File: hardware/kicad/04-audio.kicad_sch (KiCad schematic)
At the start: 9 parts, among them U5 PAM8403

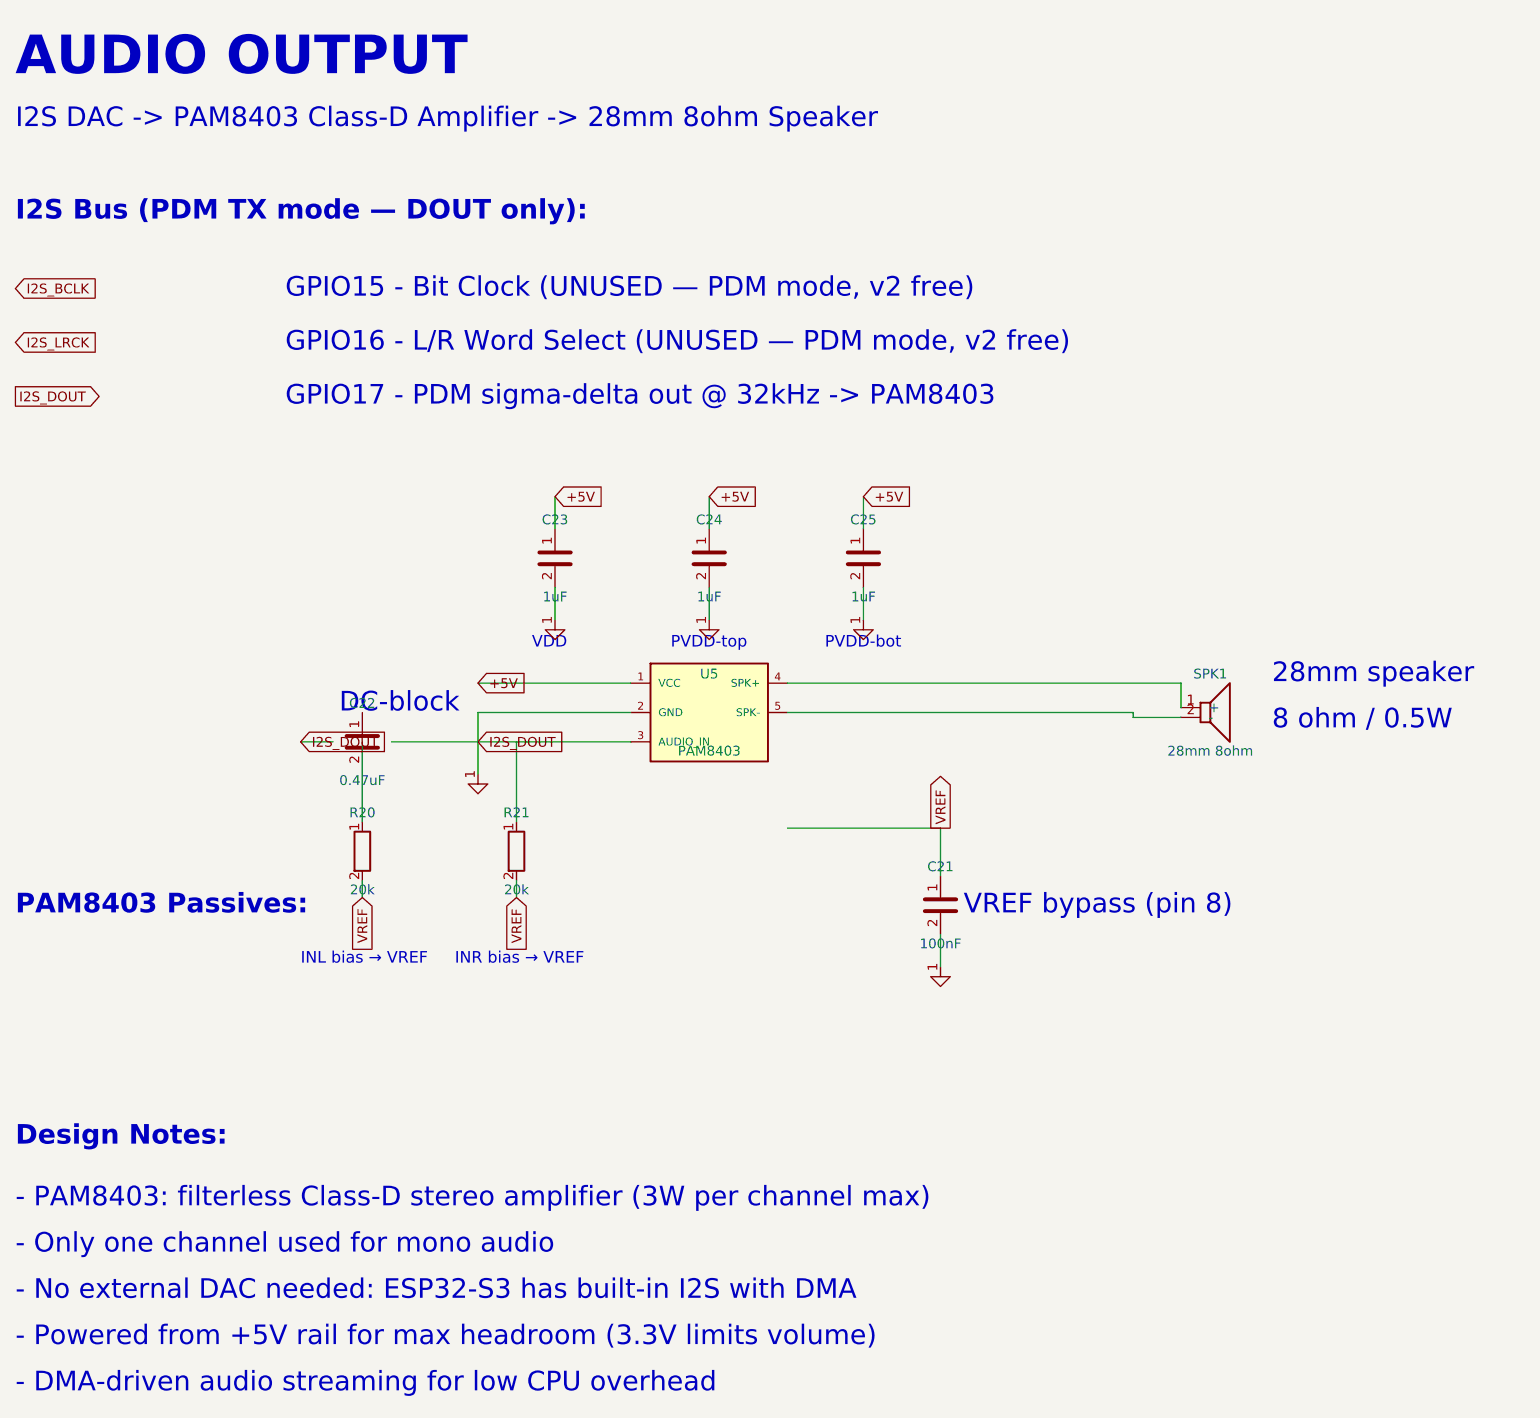
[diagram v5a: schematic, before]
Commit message: fix(pcb): R5-CRIT-6 relocate D1 so the menu combo works + split I2S_DOUT/PAM_IN_AC
Two long-standing tech-debt items, both of which were hiding real DRC
signal behind permanently-accepted "unconnected" entries.

1) R5-CRIT-6 — D1 menu-combo diode had both anodes isolated
--------------------------------------------------------------
Root cause was the placement, not the routing. D1 sat at (156, 52.5)
next to SW13, but BTN_START and BTN_SELECT both terminate around
x=100-102 and no corridor reaches x=156: the south perimeter at
y=73.955 crosses the J1 USB-C back-row shield pads (y=[72.575,74.575]),
and the north path is blocked by IP5306, L1, the regulator, the C17-C19
pads, the MENU_K F.Cu at x=156 and the USB_D+/D- verticals at x=90-91.
Previous sessions tried to route out of that position and failed.

Fix: move D1 to the buttons so only ONE net has to cross the board.

  D1 -> (101.225, 56.5), KiCad rotation 180 deg, B.Cu — the 1.30 mm free
  channel between the BTN_START column (x=100.45) and the BTN_SELECT
  column (x=102.00). At 180 deg the SOT-23 two-pad row faces north, so
  pin 1 lands on the west column and pin 2 on the east column with no
  crossing.

    D1.1 (100.275, 55.400) -> 0.175 mm B.Cu stub east onto x=100.45.
         The BTN_START vertical is split at y=55.400 so the tap is a
         real 3-way junction, not a branch into a segment middle.
    D1.2 (102.175, 55.400) -> 0.175 mm B.Cu stub west onto x=102.00,
         and the BTN_SELECT column is extended north from y=60.00.
    D1.3 (101.225, 57.600) -> B.Cu south to (101.225, 62.400) -> via ->
         F.Cu east at y=62.400 to x=137.0 -> north to y=59.850 -> east
         across SW13 pads 1 and 2.

  The SW13 pad-3 GND via moved from (135.0, 61.55) to (135.0, 63.55):
  its 2 mm F.Cu riser occupied x=[134.85,135.15], y=[61.40,63.70] —
  straight across the only usable MENU_K corridor.

  Everything stays west of x=105 in the y=[39,59] band so it does not
  collide with the parallel SY8089A buck-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
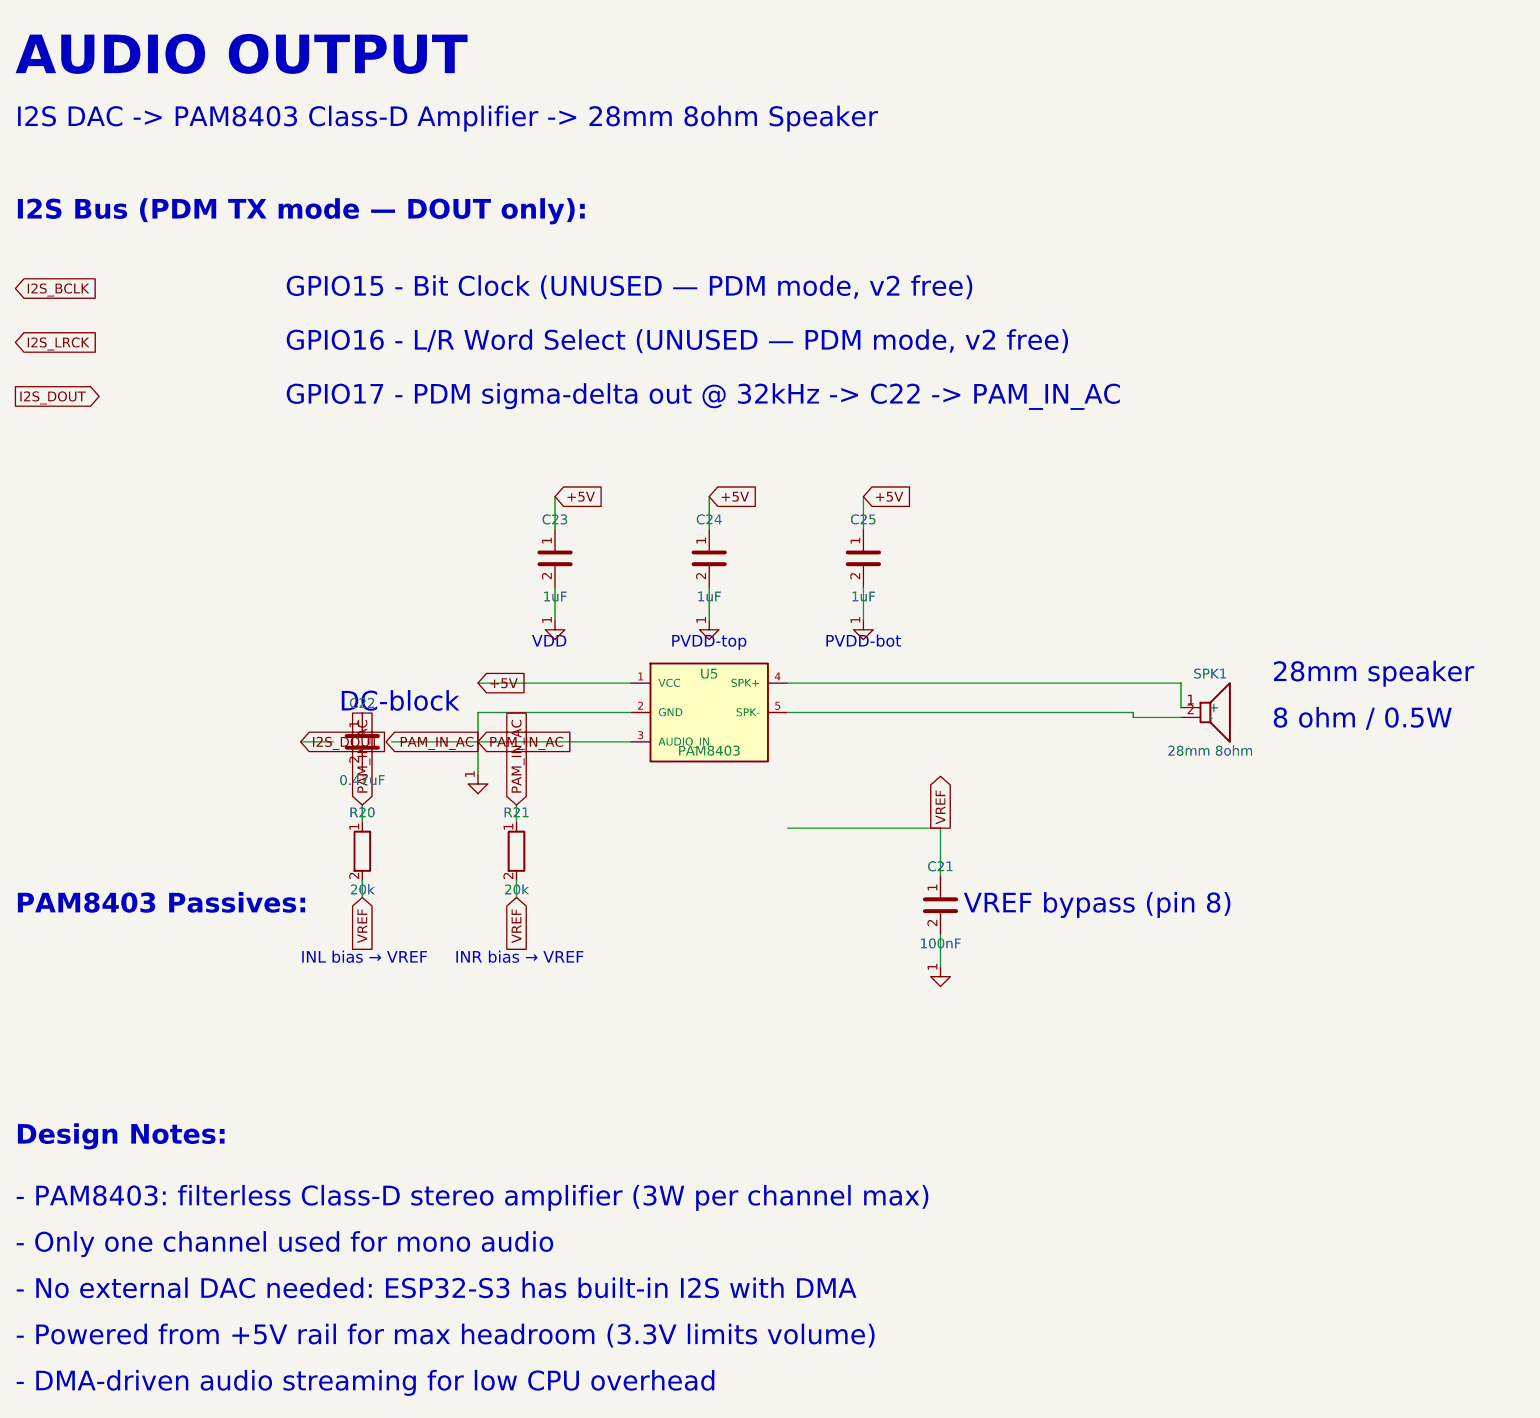
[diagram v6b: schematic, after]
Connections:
- net I2S_DOUT: no longer U5.2 (GND), U5.3 (AUDIO_IN)
- net PAM_IN_AC: now reaches R20.1
- net PAM_IN_AC: now also R21.1, U5.2 (GND), U5.3 (AUDIO_IN)
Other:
- note added: "GPIO17 - PDM sigma-delta out @ 32kHz -> C22 -> PAM_IN_AC"
- note removed: "GPIO17 - PDM sigma-delta out @ 32kHz -> PAM8403"
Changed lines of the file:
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@@
   (wire (pts (xy 109.84 110) (xy 90 110)) (stroke (width 0) (type default)))
   (wire (pts (xy 90 110) (xy 90 118)) (stroke (width 0) (type default)))
-  (global_label "I2S_DOUT" (shape input) (at 90 113.81 0) (effects (font (size 1.27 1.27))) (property "Intersheetrefs" "" (at 0 0 0) (effects (font (size 1.27 1.27)) hide)))
+  (global_label "PAM_IN_AC" (shape input) (at 90 113.81 0) (effects (font (size 1.27 1.27))) (property "Intersheetrefs" "" (at 0 0 0) (effects (font (size 1.27 1.27)) hide)))
   (wire (pts (xy 90 113.81) (xy 109.84 113.81)) (stroke (width 0) (type default)))
   (text "I2S Bus (PDM TX mode — DOUT only):" (at 30 45 0) (effects (font (size 2.54 2.54) bold) (justify left)))
@@
   (text "GPIO16 - L/R Word Select (UNUSED — PDM mode, v2 free)" (at 65 62 0) (effects (font (size 2.54 2.54)) (justify left)))
   (global_label "I2S_DOUT" (shape output) (at 30 69 0) (effects (font (size 1.27 1.27))) (property "Intersheetrefs" "" (at 0 0 0) (effects (font (size 1.27 1.27)) hide)))
-  (text "GPIO17 - PDM sigma-delta out @ 32kHz -> PAM8403" (at 65 69 0) (effects (font (size 2.54 2.54)) (justify left)))
+  (text "GPIO17 - PDM sigma-delta out @ 32kHz -> C22 -> PAM_IN_AC" (at 65 69 0) (effects (font (size 2.54 2.54)) (justify left)))
   (symbol (lib_id "Speaker") (at 185 110 0) (unit 1) (exclude_from_sim no) (in_bom yes) (on_board yes) (dnp no) (property "Reference" "SPK1" (at 185 105 0) (effects (font (size 1.27 1.27)))) (property "Value" "28mm 8ohm" (at 185 115 0) (effects (font (size 1.27 1.27)))) (pin "1") (pin "2"))
   (text "28mm speaker" (at 193 105 0) (effects (font (size 2.54 2.54)) (justify left)))
@@
   (symbol (lib_id "C") (at 75 113.81 0) (unit 1) (exclude_from_sim no) (in_bom yes) (on_board yes) (dnp no) (property "Reference" "C22" (at 75 108.81 0) (effects (font (size 1.27 1.27)))) (property "Value" "0.47uF" (at 75 118.81 0) (effects (font (size 1.27 1.27)))) (pin "1") (pin "2"))
   (wire (pts (xy 78.81 113.81) (xy 90 113.81)) (stroke (width 0) (type default)))
+  (global_label "PAM_IN_AC" (shape output) (at 90 113.81 180) (effects (font (size 1.27 1.27))) (property "Intersheetrefs" "" (at 0 0 0) (effects (font (size 1.27 1.27)) hide)))
   (wire (pts (xy 71.19 113.81) (xy 67 113.81)) (stroke (width 0) (type default)))
   (global_label "I2S_DOUT" (shape input) (at 67 113.81 0) (effects (font (size 1.27 1.27))) (property "Intersheetrefs" "" (at 0 0 0) (effects (font (size 1.27 1.27)) hide)))
   (text "DC-block" (at 72 108.81 0) (effects (font (size 2.54 2.54)) (justify left)))
   (symbol (lib_id "R") (at 75 128 0) (unit 1) (exclude_from_sim no) (in_bom yes) (on_board yes) (dnp no) (property "Reference" "R20" (at 75 123 0) (effects (font (size 1.27 1.27)))) (property "Value" "20k" (at 75 133 0) (effects (font (size 1.27 1.27)))) (pin "1") (pin "2"))
-  (wire (pts (xy 75 124.19) (xy 75 113.81)) (stroke (width 0) (type default)))
+  (wire (pts (xy 75 124.19) (xy 75 122)) (stroke (width 0) (type default)))
+  (global_label "PAM_IN_AC" (shape input) (at 75 122 90) (effects (font (size 1.27 1.27))) (property "Intersheetrefs" "" (at 0 0 0) (effects (font (size 1.27 1.27)) hide)))
   (wire (pts (xy 75 131.81) (xy 75 134)) (stroke (width 0) (type default)))
   (global_label "VREF" (shape input) (at 75 134 270) (effects (font (size 1.27 1.27))) (property "Intersheetrefs" "" (at 0 0 0) (effects (font (size 1.27 1.27)) hide)))
   (text "INL bias → VREF" (at 67 142 0) (effects (font (size 1.5 1.5)) (justify left)))
   (symbol (lib_id "R") (at 95 128 0) (unit 1) (exclude_from_sim no) (in_bom yes) (on_board yes) (dnp no) (property "Reference" "R21" (at 95 123 0) (effects (font (size 1.27 1.27)))) (property "Value" "20k" (at 95 133 0) (effects (font (size 1.27 1.27)))) (pin "1") (pin "2"))
-  (wire (pts (xy 95 124.19) (xy 95 113.81)) (stroke (width 0) (type default)))
+  (wire (pts (xy 95 124.19) (xy 95 122)) (stroke (width 0) (type default)))
+  (global_label "PAM_IN_AC" (shape input) (at 95 122 90) (effects (font (size 1.27 1.27))) (property "Intersheetrefs" "" (at 0 0 0) (effects (font (size 1.27 1.27)) hide)))
   (wire (pts (xy 95 131.81) (xy 95 134)) (stroke (width 0) (type default)))
   (global_label "VREF" (shape input) (at 95 134 270) (effects (font (size 1.27 1.27))) (property "Intersheetrefs" "" (at 0 0 0) (effects (font (size 1.27 1.27)) hide)))
